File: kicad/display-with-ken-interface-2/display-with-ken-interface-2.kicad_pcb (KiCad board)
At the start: 4 copper layers, 50.8 x 81.3 mm, 10 parts, among them J1 Conn_01x07_Pin, J4 TFT_SPI, J5 Conn_01x08_Pin, U3 XDZ254-2-15-W-2.5-G1, U5 PM254-2-15-W-8.5

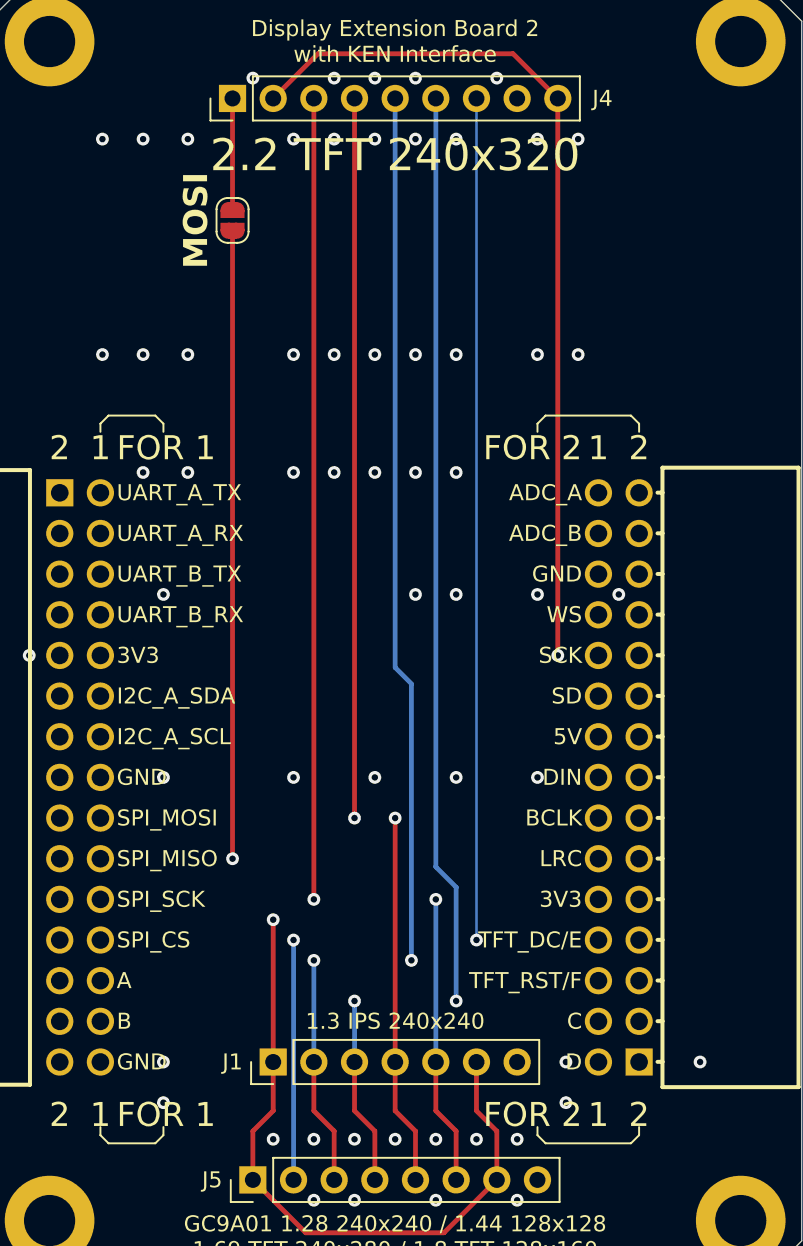
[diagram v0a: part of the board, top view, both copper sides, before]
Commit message: new display board send to pcb maker
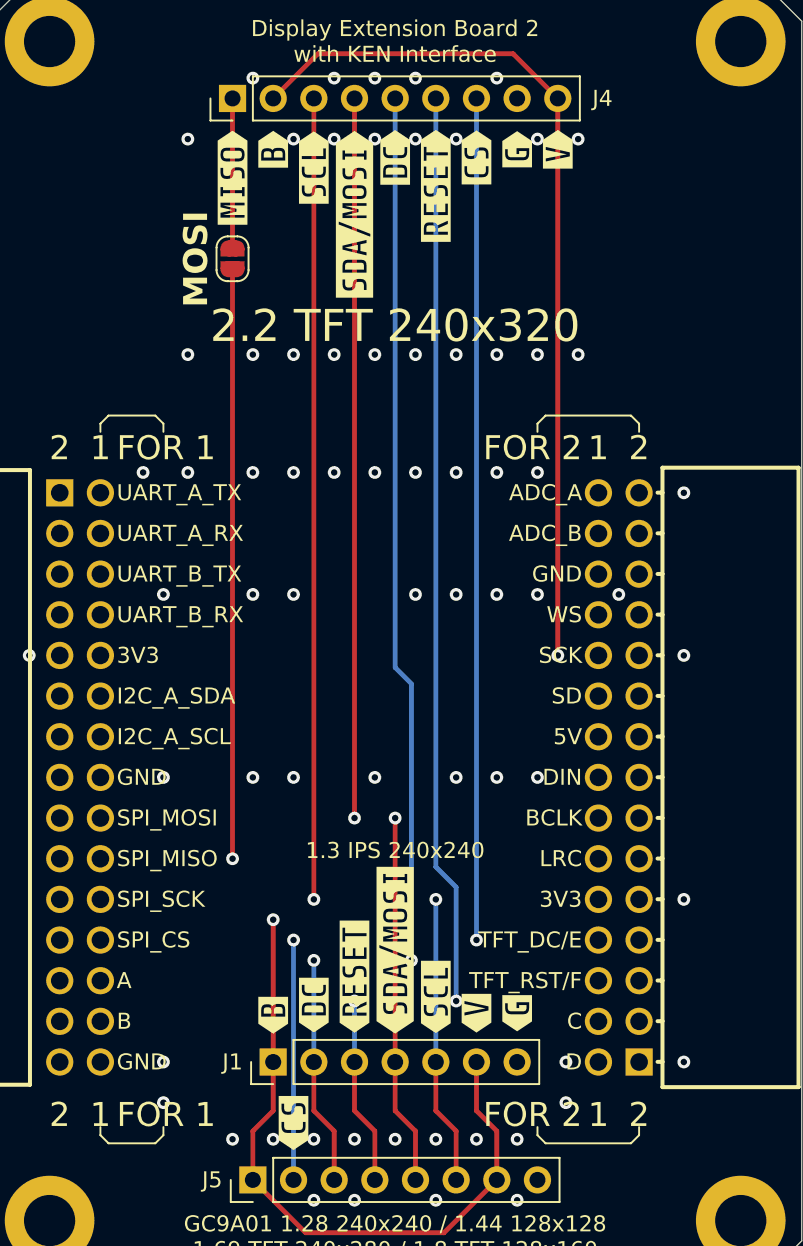
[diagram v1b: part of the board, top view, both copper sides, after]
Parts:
- added kibuzzard-69E8720F: G***, kibuzzard-69E8720F, F.Cu at (91.4, 103.9)
- added kibuzzard-69E87221: G***, kibuzzard-69E87221, F.Cu at (76.2, 104.0)
- added kibuzzard-69E87232: G***, kibuzzard-69E87232, F.Cu at (86.4, 102.9)
- added kibuzzard-69E8724B: G***, kibuzzard-69E8724B, F.Cu at (83.8, 99.9)
- added kibuzzard-69E8725D: G***, kibuzzard-69E8725D, F.Cu at (81.3, 101.6)
- added kibuzzard-69E87269: G***, kibuzzard-69E87269, F.Cu at (78.7, 103.4)
- added kibuzzard-69E872B6: G***, kibuzzard-69E872B6, F.Cu at (88.9, 103.9)
- added kibuzzard-69E872D5: G***, kibuzzard-69E872D5, F.Cu at (77.5, 110.7)
- added kibuzzard-69E87476: G***, kibuzzard-69E87476, F.Cu at (73.7, 51.7)
- added kibuzzard-69E8747C: G***, kibuzzard-69E8747C, F.Cu at (76.2, 49.9)
- added kibuzzard-69E87482: G***, kibuzzard-69E87482, F.Cu at (78.7, 51.1)
- added kibuzzard-69E87487: G***, kibuzzard-69E87487, F.Cu at (81.3, 54.0)
- added kibuzzard-69E8749A: G***, kibuzzard-69E8749A, F.Cu at (83.8, 50.4)
- added kibuzzard-69E874A0: G***, kibuzzard-69E874A0, F.Cu at (86.4, 52.2)
- added kibuzzard-69E874A4: G***, kibuzzard-69E874A4, F.Cu at (88.9, 50.4)
- added kibuzzard-69E874AD: G***, kibuzzard-69E874AD, F.Cu at (94.0, 49.9)
- added kibuzzard-69E874B2: G***, kibuzzard-69E874B2, F.Cu at (91.4, 49.9)
- moved JP1 2.40 mm to (73.7, 56.8)
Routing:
- net TFT_MISO: track 6.97 -> 9.37 mm
- net /IO13: track 70.3 -> 67.9 mm
- net GC9A01_GND: vias 63 -> 73
